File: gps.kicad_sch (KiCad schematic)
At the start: 18 parts, among them J6 SMA, Q1 AO3400A, Q2 AO3401A, U1 MAX-M10S, U15 74LVC1G07

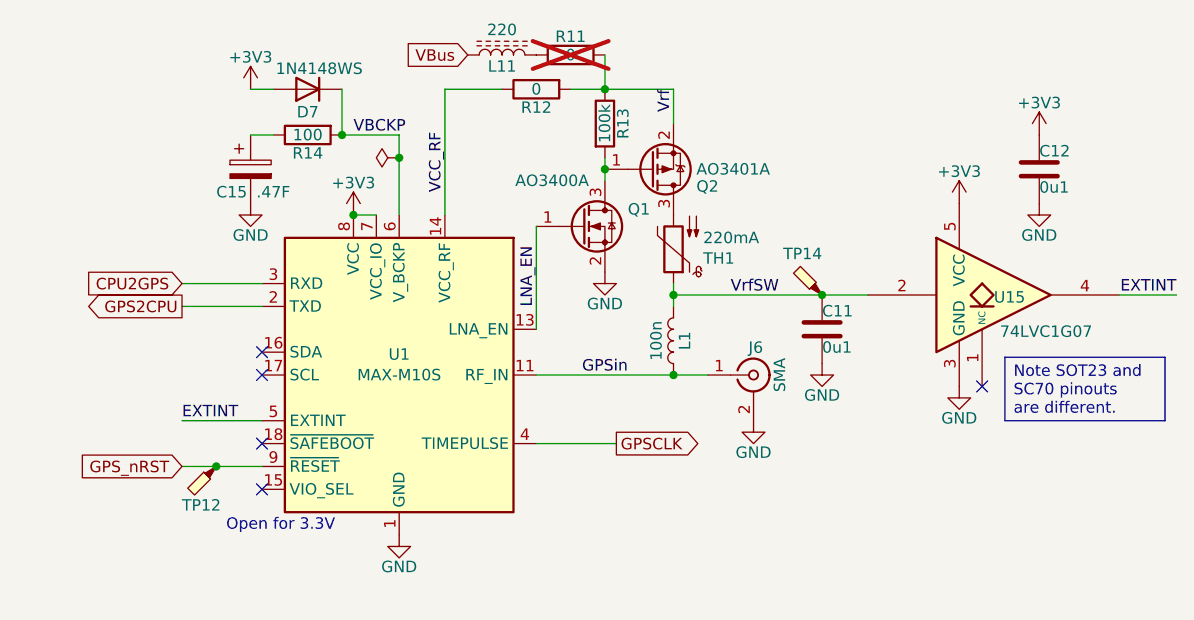
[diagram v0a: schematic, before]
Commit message: Squeeze in a connector to break out GPS.
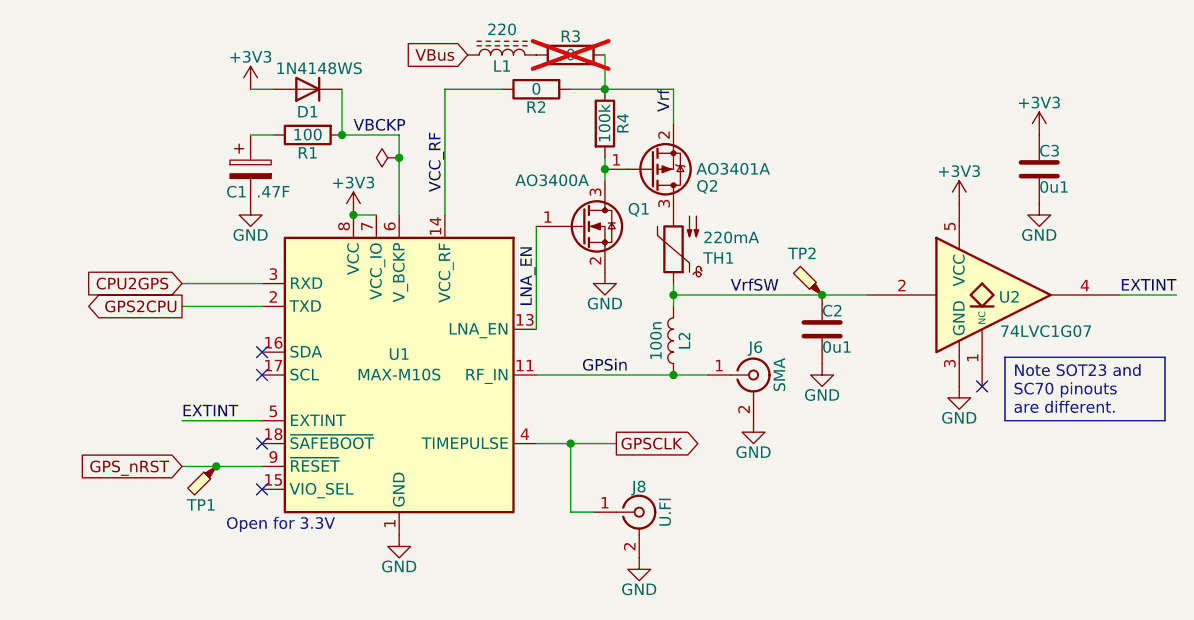
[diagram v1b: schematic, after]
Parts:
- added J8: U.Fl, Parts:U.FL_Hirose_U.FL-R-SMT-1_Vertical, symbol Connector:Conn_Coaxial
- renumbered C15 to C1, C11 to C2, C12 to C3, D7 to D1, L11 to L1, L1 to L2, R14 to R1, R12 to R2, R11 to R3, R13 to R4, TP12 to TP1, TP14 to TP2, U15 to U2
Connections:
- net GND: now also J8.2 (Ext)
- net GPSCLK: now also J8.1 (In)

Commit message: Silkscreen passes DRC.  Also we renumbered everything.
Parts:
- U11: renamed from U2; footprint Package_TO_SOT_SMD:SOT-23-5 -> Parts:SOT-23-5
- renumbered C2 to C11, C1 to C12, C3 to C13, R2 to R11, R4 to R12, R1 to R13, R3 to R14
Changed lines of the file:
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@@
 		(on_board yes)
 		(dnp no)
-		(property "Reference" "C1"
+		(property "Reference" "C12"
 			(at 83.439 78.74 0)
 			(effects
@@
 			(project ""
 				(path "/3160ff17-81c2-4674-af97-e8d9acaf6b65/69331f4b-e5ad-4452-8850-5c5a77857efb"
-					(reference "C1")
+					(reference "C12")
 					(unit 1)
 				)
@@
 		(on_board yes)
 		(dnp yes)
-		(property "Reference" "R3"
+		(property "Reference" "R14"
 			(at 119.38 61.468 90)
 			(effects
@@
 			(project "gpsref"
 				(path "/3160ff17-81c2-4674-af97-e8d9acaf6b65/69331f4b-e5ad-4452-8850-5c5a77857efb"
-					(reference "R3")
+					(reference "R14")
 					(unit 1)
 				)
@@
 		(on_board yes)
 		(dnp no)
-		(property "Reference" "R1"
+		(property "Reference" "R13"
 			(at 90.17 74.422 90)
 			(effects
@@
 			(project "gpsref"
 				(path "/3160ff17-81c2-4674-af97-e8d9acaf6b65/69331f4b-e5ad-4452-8850-5c5a77857efb"
-					(reference "R1")
+					(reference "R13")
 					(unit 1)
 				)
@@
 		(on_board yes)
 		(dnp no)
-		(property "Reference" "U2"
+		(property "Reference" "U11"
 			(at 168.148 90.424 0)
 			(effects
@@
 			)
 		)
-		(property "Footprint" "Package_TO_SOT_SMD:SOT-23-5"
+		(property "Footprint" "Parts:SOT-23-5"
 			(at 167.64 90.17 0)
 			(effects
@@
 			(project "gpsref"
 				(path "/3160ff17-81c2-4674-af97-e8d9acaf6b65/69331f4b-e5ad-4452-8850-5c5a77857efb"
-					(reference "U2")
+					(reference "U11")
 					(unit 1)
 				)
@@
 		(on_board yes)
 		(dnp no)
-		(property "Reference" "R2"
+		(property "Reference" "R11"
 			(at 115.57 69.342 90)
 			(effects
@@
 			(project "gpsref"
 				(path "/3160ff17-81c2-4674-af97-e8d9acaf6b65/69331f4b-e5ad-4452-8850-5c5a77857efb"
-					(reference "R2")
+					(reference "R11")
 					(unit 1)
 				)
@@
 		(on_board yes)
 		(dnp no)
-		(property "Reference" "C3"
+		(property "Reference" "C13"
 			(at 171.45 74.93 0)
 			(effects
@@
 			(project "gpsref"
 				(path "/3160ff17-81c2-4674-af97-e8d9acaf6b65/69331f4b-e5ad-4452-8850-5c5a77857efb"
-					(reference "C3")
+					(reference "C13")
 					(unit 1)
 				)
@@
 		(on_board yes)
 		(dnp no)
-		(property "Reference" "C2"
+		(property "Reference" "C11"
 			(at 147.32 92.71 0)
 			(effects
@@
 			(project "gpsref"
 				(path "/3160ff17-81c2-4674-af97-e8d9acaf6b65/69331f4b-e5ad-4452-8850-5c5a77857efb"
-					(reference "C2")
+					(reference "C11")
 					(unit 1)
 				)
@@
 		(on_board yes)
 		(dnp no)
-		(property "Reference" "R4"
+		(property "Reference" "R12"
 			(at 125.222 71.12 90)
 			(effects
@@
 			(project "gpsref"
 				(path "/3160ff17-81c2-4674-af97-e8d9acaf6b65/69331f4b-e5ad-4452-8850-5c5a77857efb"
-					(reference "R4")
-					(unit 1)
-				)
+					(reference "R12")
+					(unit 1)
+				)

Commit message: Sorting out part number assignments.
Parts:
- C11, C13: JLCPCB C307331 -> (none); LCSC (none) -> C307331
- D1: JLCPCB C2128 -> (none); LCSC (none) -> C2128
- L1: JLCPCB C14709 -> (none); LCSC (none) -> C14709
- Q1: JLCPCB C20917 -> (none); LCSC (none) -> C20917
- Q2: JLCPCB C15127 -> (none); LCSC (none) -> C15127
- R11: JLCPCB C21189 -> (none); LCSC (none) -> C21189
- R12: JLCPCB C25741 -> (none); LCSC (none) -> C25741
- R13: JLCPCB C25076 -> (none); LCSC (none) -> C25076
- R14: LCSC (none) -> C17168
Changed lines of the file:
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@@
-			)
-		)
-		(property "JLCPCB" ""
-			(at 130.81 85.09 0)
-			(effects
-				(font
-					(size 1.27 1.27)
-				)
-				(hide yes)
 			)
 		)
@@
 			)
 		)
-		(property "JLCPCB" ""
-			(at 130.81 95.25 0)
-			(effects
-				(font
-					(size 1.27 1.27)
-				)
-				(hide yes)
-			)
-		)
 		(pin "2"
 		)
@@
 			)
 		)
-		(property "JLCPCB" ""
-			(at 83.82 76.2 0)
-			(effects
-				(font
-					(size 1.27 1.27)
-				)
-				(hide yes)
-			)
-		)
 		(pin "2"
 		)
@@
 			)
 		)
-		(property "JLCPCB" "C20917"
+		(property "LCSC" "C20917"
 			(at 120.65 82.55 0)
 			(effects
@@
 			)
 		)
-		(property "JLCPCB" ""
-			(at 119.38 63.5 0)
+		(property "LCSC" "C17168"
+			(at 119.38 63.5 90)
 			(effects
 				(font
@@
 			)
 		)
-		(property "JLCPCB" "C25076"
-			(at 90.17 72.39 0)
+		(property "LCSC" "C25076"
+			(at 90.17 72.39 90)
 			(effects
 				(font
@@
 			)
 		)
-		(property "JLCPCB" "C2128"
+		(property "LCSC" "C2128"
 			(at 90.17 67.31 0)
 			(effects
@@
 			)
 		)
-		(property "JLCPCB" ""
-			(at 167.64 90.17 0)
-			(effects
-				(font
-					(size 1.27 1.27)
-				)
-				(hide yes)
-			)
-		)
 		(pin "4"
 		)
@@
 			)
 		)
-		(property "JLCPCB" "C14709"
+		(property "LCSC" "C14709"
 			(at 111.76 63.5 90)
 			(effects
@@
 			)
 		)
-		(property "JLCPCB" "C21189"
-			(at 115.57 67.31 0)
+		(property "LCSC" "C21189"
+			(at 115.57 67.31 90)
 			(effects
 				(font
@@
 			)
 		)
-		(property "JLCPCB" "C307331"
+		(property "LCSC" "C307331"
 			(at 171.45 76.2 0)
 			(effects
@@
 			)
 		)
-		(property "JLCPCB" "C307331"
+		(property "LCSC" "C307331"
 			(at 147.32 93.98 0)
 			(effects
@@
 			)
 		)
-		(property "JLCPCB" "C15127"
+		(property "LCSC" "C15127"
 			(at 128.27 76.2 0)
 			(effects
@@
 			)
 		)
-		(property "JLCPCB" "C25741"
+		(property "LCSC" "C25741"
 			(at 123.19 71.12 90)
 			(effects
@@
 			(at 127 114.3 0)
 			(effects
-				(font
-					(size 1.27 1.27)
-				)
-				(hide yes)
-			)
-		)
-		(property "JLCPCB" ""
-			(at 127 114.3 0)
-			(effects

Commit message: Final fixes.  Ordered.
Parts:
- R14: now left out of the parts list
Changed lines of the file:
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@@
 		(unit 1)
 		(exclude_from_sim no)
-		(in_bom yes)
+		(in_bom no)
 		(on_board yes)
 		(dnp yes)
@@
 			(effects
 				(font
+					(size 1.27 1.27)
+				)
+				(hide yes)
+			)
+		)
+		(property "JLCPCB" ""
+			(at 119.38 63.5 0)
+			(effects
+				(font

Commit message: Change the programming connector.
Change the SMA footprint to match narrow ones.
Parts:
- J6: footprint Parts:SMA_Amphenol_132289_EdgeMount -> Parts:SMA_EdgeMount
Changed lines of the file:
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@@
 			)
 		)
-		(property "Footprint" "Parts:SMA_Amphenol_132289_EdgeMount"
+		(property "Footprint" "Parts:SMA_EdgeMount"
 			(at 139.7 99.06 0)
 			(effects
@@
 		(dnp no)
 		(property "Reference" "U11"
-			(at 168.148 90.424 0)
-			(effects
-				(font
+			(at 168.91 90.17 0)
+			(effects
+				(font

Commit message: Ready for respin.
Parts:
- R14: LCSC C17168 -> (none)
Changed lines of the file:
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@@
 			)
 		)
-		(property "LCSC" "C17168"
+		(property "LCSC" ""
 			(at 119.38 63.5 90)
 			(effects

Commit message: Schematic updates for revision mostly done.
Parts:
- added C11: 10u, Capacitor_SMD:C_0402_1005Metric, symbol Device:C
- added C13: 0u1, Capacitor_SMD:C_0402_1005Metric, symbol Device:C
- added L11: 220, Inductor_SMD:L_0603_1608Metric, symbol Parts:L_Ferrite_Power
- renumbered C11 to C14, C13 to C15, L2 to L1, L1 to L3, R13 to R11, R11 to R12, R14 to R13, R12 to R14
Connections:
- net +3V3: now also L11.1; no longer C15.1, D1.2 (A), U1.7 (VCC_IO), U1.8 (VCC), U11.5 (VCC)
- net GND: now also C11.2, C13.2
- net VBCKP: now also C13.1
- new net VGPS: C11.1, C15.1, D1.2 (A), L11.2, U1.7 (VCC_IO), U1.8 (VCC), U11.5 (VCC)
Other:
- moved on the sheet: C12, C15, J8, R11, U11
